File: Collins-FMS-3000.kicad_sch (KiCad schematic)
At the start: 29 parts, among them U2 MCP23017_SO, U3 MCP23017_SO, U4 IS31FL3733B

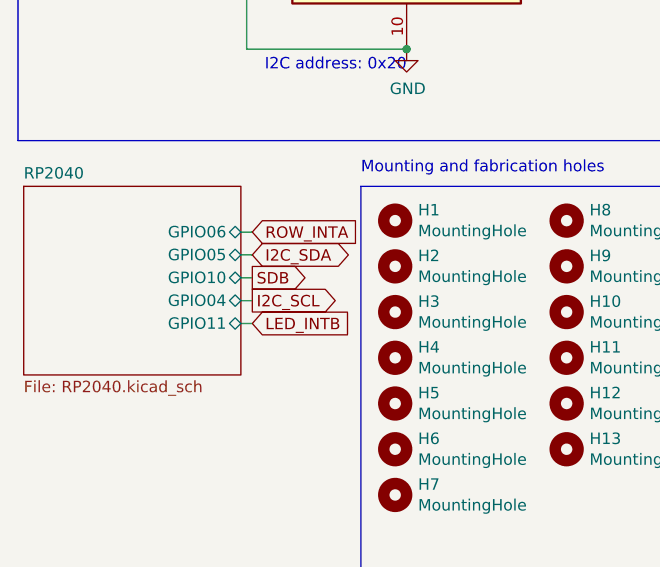
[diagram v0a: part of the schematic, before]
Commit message: Correct pin assignment for I2C, add via stitching
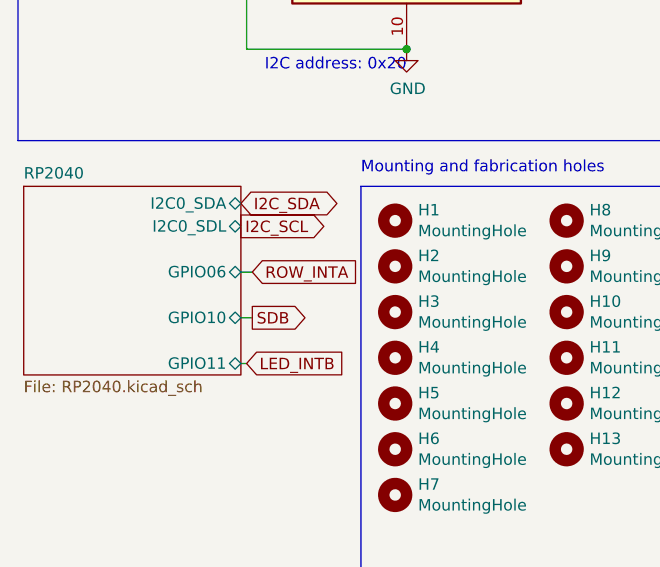
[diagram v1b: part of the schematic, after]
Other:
- sheet RP2040 ports: added I2C0_SDA, I2C0_SDL; removed GPIO04, GPIO05
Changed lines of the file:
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@@
     (stroke (width 0) (type default) (color 0 0 0 0))
   )
-  (wire (pts (xy 38.735 101.6) (xy 40.005 101.6))
+  (wire (pts (xy 38.735 106.045) (xy 40.005 106.045))
     (stroke (width 0) (type default) (color 0 0 0 0))
   )
@@
     (stroke (width 0) (type default) (color 0 0 0 0))
   )
-  (wire (pts (xy 38.735 106.68) (xy 40.005 106.68))
+  (wire (pts (xy 38.735 111.125) (xy 40.005 111.125))
     (stroke (width 0) (type default) (color 0 0 0 0))
   )
@@
     (stroke (width 0) (type default) (color 0 0 0 0))
   )
-  (wire (pts (xy 40.005 109.22) (xy 38.735 109.22))
-    (stroke (width 0) (type default) (color 0 0 0 0))
-  )
   (wire (pts (xy 148.59 27.94) (xy 153.67 27.94))
     (stroke (width 0) (type default) (color 0 0 0 0))
@@
     (stroke (width 0) (type default) (color 0 0 0 0))
   )
-  (wire (pts (xy 38.735 104.14) (xy 40.005 104.14))
-    (stroke (width 0) (type default) (color 0 0 0 0))
-  )
   (wire (pts (xy 148.59 22.86) (xy 138.43 22.86))
     (stroke (width 0) (type default) (color 0 0 0 0))
@@
     (stroke (width 0) (type default) (color 0 0 0 0))
   )
-  (wire (pts (xy 40.005 111.76) (xy 38.735 111.76))
+  (wire (pts (xy 39.37 116.205) (xy 38.735 116.205))
     (stroke (width 0) (type default) (color 0 0 0 0))
   )
@@
     )
   )
-  (global_label "LED_INTB" (shape input) (at 40.005 111.76 0) (fields_autoplaced)
+  (global_label "LED_INTB" (shape input) (at 39.37 116.205 0) (fields_autoplaced)
     (effects (font (size 1.27 1.27)) (justify left))
-    (property "Intersheet References" "${INTERSHEET_REFS}" (id 0) (at 0.635 1.27 0)
+    (property "Intersheet References" "${INTERSHEET_REFS}" (id 0) (at 0 5.715 0)
       (effects (font (size 1.27 1.27)) hide)
     )
@@
     )
   )
-  (global_label "ROW_INTA" (shape input) (at 40.005 101.6 0) (fields_autoplaced)
+  (global_label "ROW_INTA" (shape input) (at 40.005 106.045 0) (fields_autoplaced)
     (effects (font (size 1.27 1.27)) (justify left))
-    (property "Intersheet References" "${INTERSHEET_REFS}" (id 0) (at 0.635 -11.43 0)
+    (property "Intersheet References" "${INTERSHEET_REFS}" (id 0) (at 0.635 -6.985 0)
       (effects (font (size 1.27 1.27)) hide)
     )
@@
     )
   )
-  (global_label "I2C_SDA" (shape bidirectional) (at 40.005 104.14 0) (fields_autoplaced)
+  (global_label "I2C_SDA" (shape bidirectional) (at 38.735 98.425 0) (fields_autoplaced)
     (effects (font (size 1.27 1.27)) (justify left))
-    (property "Intersheet References" "${INTERSHEET_REFS}" (id 0) (at 0.635 1.27 0)
-      (effects (font (size 1.27 1.27)) hide)
-    )
-  )
-  (global_label "I2C_SCL" (shape output) (at 40.005 109.22 0) (fields_autoplaced)
+    (property "Intersheet References" "${INTERSHEET_REFS}" (id 0) (at -0.635 -4.445 0)
+      (effects (font (size 1.27 1.27)) hide)
+    )
+  )
+  (global_label "I2C_SCL" (shape output) (at 38.735 100.965 0) (fields_autoplaced)
     (effects (font (size 1.27 1.27)) (justify left))
-    (property "Intersheet References" "${INTERSHEET_REFS}" (id 0) (at 0.635 3.81 0)
-      (effects (font (size 1.27 1.27)) hide)
-    )
-  )
-  (global_label "SDB" (shape output) (at 40.005 106.68 0) (fields_autoplaced)
+    (property "Intersheet References" "${INTERSHEET_REFS}" (id 0) (at -0.635 -4.445 0)
+      (effects (font (size 1.27 1.27)) hide)
+    )
+  )
+  (global_label "SDB" (shape output) (at 40.005 111.125 0) (fields_autoplaced)
     (effects (font (size 1.27 1.27)) (justify left))
-    (property "Intersheet References" "${INTERSHEET_REFS}" (id 0) (at 0.635 -1.27 0)
+    (property "Intersheet References" "${INTERSHEET_REFS}" (id 0) (at 0.635 3.175 0)
       (effects (font (size 1.27 1.27)) hide)
     )
@@
       (effects (font (size 1.27 1.27)) (justify left top))
     )
-    (pin "GPIO06" bidirectional (at 38.735 101.6 0)
-      (effects (font (size 1.27 1.27)) (justify right))
-    )
-    (pin "GPIO05" bidirectional (at 38.735 104.14 0)
-      (effects (font (size 1.27 1.27)) (justify right))
-    )
-    (pin "GPIO04" bidirectional (at 38.735 109.22 0)
-      (effects (font (size 1.27 1.27)) (justify right))
-    )
-    (pin "GPIO11" bidirectional (at 38.735 111.76 0)
-      (effects (font (size 1.27 1.27)) (justify right))
-    )
-    (pin "GPIO10" bidirectional (at 38.735 106.68 0)
-      (effects (font (size 1.27 1.27)) (justify right))
-    )
+    (pin "GPIO06" bidirectional (at 38.735 106.045 0)
+      (effects (font (size 1.27 1.27)) (justify right))
+    )
+    (pin "GPIO11" bidirectional (at 38.735 116.205 0)
+      (effects (font (size 1.27 1.27)) (justify right))
+    )
+    (pin "GPIO10" bidirectional (at 38.735 111.125 0)
+      (effects (font (size 1.27 1.27)) (justify right))
+    )
+    (pin "I2C0_SDL" bidirectional (at 38.735 100.965 0)
+      (effects (font (size 1.27 1.27)) (justify right))
+    )
+    (pin "I2C0_SDA" bidirectional (at 38.735 98.425 0)
+      (effects (font (size 1.27 1.27)) (justify right))
+    )

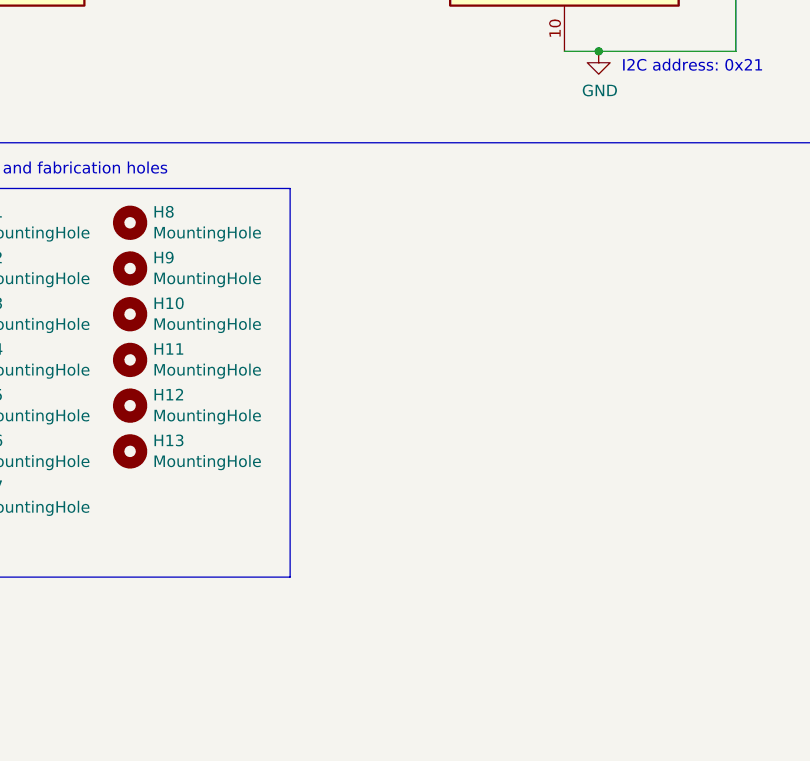
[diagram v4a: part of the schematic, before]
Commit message: Add test points
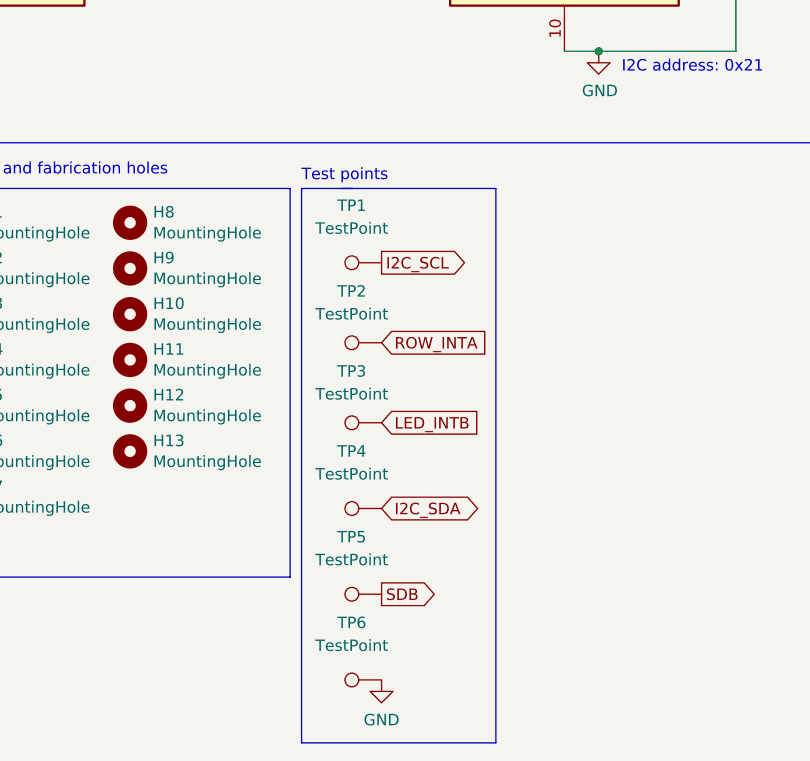
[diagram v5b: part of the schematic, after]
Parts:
- added TP1, TP2, TP3, TP4, TP5, TP6: TestPoint, TestPoint:TestPoint_Keystone_5005-5009_Compact, symbol Connector:TestPoint
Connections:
- net GND: now also TP6.1
- net I2C_SCL: now also TP1.1
- net I2C_SDA: now also TP4.1
- net LED_INTB: now also TP3.1
- net ROW_INTA: now also TP2.1
- net SDB: now also TP5.1
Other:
- note added: "Test points"
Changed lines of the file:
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@@
+    (stroke (width 0) (type default) (color 0 0 0 0))
+  )
+  (polyline (pts (xy 93.98 96.52) (xy 93.98 158.115))
     (stroke (width 0) (type default) (color 0 0 0 0))
   )
@@
     (stroke (width 0) (type default) (color 0 0 0 0))
   )
+  (polyline (pts (xy 99.695 96.52) (xy 93.98 96.52))
+    (stroke (width 0) (type default) (color 0 0 0 0))
+  )
   (wire (pts (xy 101.6 40.64) (xy 105.41 40.64))
     (stroke (width 0) (type default) (color 0 0 0 0))
@@
     (stroke (width 0) (type default) (color 0 0 0 0))
   )
+  (polyline (pts (xy 93.98 158.115) (xy 115.57 158.115))
+    (stroke (width 0) (type default) (color 0 0 0 0))
+  )
   (wire (pts (xy 214.63 62.23) (xy 222.25 62.23))
     (stroke (width 0) (type default) (color 0 0 0 0))
@@
     (stroke (width 0) (type default) (color 0 0 0 0))
   )
+  (polyline (pts (xy 98.425 96.52) (xy 115.57 96.52))
+    (stroke (width 0) (type default) (color 0 0 0 0))
+  )
   (wire (pts (xy 182.88 33.02) (xy 172.72 33.02))
     (stroke (width 0) (type default) (color 0 0 0 0))
@@
   )
   (polyline (pts (xy 52.07 96.52) (xy 92.71 96.52))
+    (stroke (width 0) (type default) (color 0 0 0 0))
+  )
+  (polyline (pts (xy 115.57 158.115) (xy 115.57 96.52))
     (stroke (width 0) (type default) (color 0 0 0 0))
   )
@@
     (effects (font (size 1.27 1.27)) (justify right bottom))
   )
+  (text "Test points" (at 93.98 95.885 0)
+    (effects (font (size 1.27 1.27)) (justify left bottom))
+  )
   (text "Button matrix" (at 13.97 15.24 0)
     (effects (font (size 1.27 1.27)) (justify left bottom))
@@
   (text "Backlight LEDs" (at 160.02 15.24 0)
     (effects (font (size 1.27 1.27)) (justify left bottom))
+  )
+  (global_label "I2C_SCL" (shape output) (at 102.87 104.775 0) (fields_autoplaced)
+    (effects (font (size 1.27 1.27)) (justify left))
+    (property "Intersheet References" "${INTERSHEET_REFS}" (id 0) (at 112.7537 104.6956 0)
+      (effects (font (size 1.27 1.27)) (justify left) hide)
+    )
   )
   (global_label "I2C_SCL" (shape input) (at 140.97 35.56 0) (fields_autoplaced)
@@
     )
   )
+  (global_label "I2C_SDA" (shape bidirectional) (at 102.87 132.08 0) (fields_autoplaced)
+    (effects (font (size 1.27 1.27)) (justify left))
+    (property "Intersheet References" "${INTERSHEET_REFS}" (id 0) (at 112.8142 132.0006 0)
+      (effects (font (size 1.27 1.27)) (justify left) hide)
+    )
+  )
   (global_label "LED_INTB" (shape input) (at 39.37 116.205 0) (fields_autoplaced)
     (effects (font (size 1.27 1.27)) (justify left))
@@
     )
   )
+  (global_label "ROW_INTA" (shape input) (at 102.87 113.665 0) (fields_autoplaced)
+    (effects (font (size 1.27 1.27)) (justify left))
+    (property "Intersheet References" "${INTERSHEET_REFS}" (id 0) (at 114.2052 113.5856 0)
+      (effects (font (size 1.27 1.27)) (justify left) hide)
+    )
+  )
   (global_label "I2C_SDA" (shape bidirectional) (at 39.37 33.02 180) (fields_autoplaced)
     (effects (font (size 1.27 1.27)) (justify right))
@@
     )
   )
+  (global_label "SDB" (shape output) (at 102.87 141.605 0) (fields_autoplaced)
+    (effects (font (size 1.27 1.27)) (justify left))
+    (property "Intersheet References" "${INTERSHEET_REFS}" (id 0) (at 108.9437 141.5256 0)
+      (effects (font (size 1.27 1.27)) (justify left) hide)
+    )
+  )
   (global_label "ROW_INTA" (shape input) (at 40.005 106.045 0) (fields_autoplaced)
     (effects (font (size 1.27 1.27)) (justify left))
@@
     (property "Intersheet References" "${INTERSHEET_REFS}" (id 0) (at 0 0 0)
       (effects (font (size 1.27 1.27)) hide)
+    )
+  )
+  (global_label "LED_INTB" (shape input) (at 102.87 122.555 0) (fields_autoplaced)
+    (effects (font (size 1.27 1.27)) (justify left))
+    (property "Intersheet References" "${INTERSHEET_REFS}" (id 0) (at 113.7818 122.4756 0)
+      (effects (font (size 1.27 1.27)) (justify left) hide)
     )
   )
@@
     (pin "1")
   )
+  (symbol (lib_id "Connector:TestPoint") (at 102.87 122.555 90) (unit 1)
+    (in_bom yes) (on_board yes) (fields_autoplaced)
+    (property "Reference" "TP3" (id 0) (at 99.568 116.84 90))
+    (property "Value" "TestPoint" (id 1) (at 99.568 119.38 90))
+    (property "Footprint" "TestPoint:TestPoint_Keystone_5005-5009_Compact" (id 2) (at 102.87 117.475 0)
+      (effects (font (size 1.27 1.27)) hide)
+    )
+    (property "Datasheet" "~" (id 3) (at 102.87 117.475 0)
+      (effects (font (size 1.27 1.27)) hide)
+    )
+    (pin "1")
+  )
+  (symbol (lib_id "power:GND") (at 102.87 151.13 0) (unit 1)
+    (in_bom yes) (on_board yes) (fields_autoplaced)
+    (property "Reference" "#PWR01" (id 0) (at 102.87 157.48 0)
+      (effects (font (size 1.27 1.27)) hide)
+    )
+    (property "Value" "GND" (id 1) (at 102.87 155.575 0))
+    (property "Footprint" "" (id 2) (at 102.87 151.13 0)
+      (effects (font (size 1.27 1.27)) hide)
+    )
+    (property "Datasheet" "" (id 3) (at 102.87 151.13 0)
+      (effects (font (size 1.27 1.27)) hide)
+    )
+    (pin "1")
+  )
+  (symbol (lib_id "Connector:TestPoint") (at 102.87 104.775 90) (unit 1)
+    (in_bom yes) (on_board yes) (fields_autoplaced)
+    (property "Reference" "TP1" (id 0) (at 99.568 98.425 90))
+    (property "Value" "TestPoint" (id 1) (at 99.568 100.965 90))
+    (property "Footprint" "TestPoint:TestPoint_Keystone_5005-5009_Compact" (id 2) (at 102.87 99.695 0)
+      (effects (font (size 1.27 1.27)) hide)
+    )
+    (property "Datasheet" "~" (id 3) (at 102.87 99.695 0)
+      (effects (font (size 1.27 1.27)) hide)
+    )
+    (pin "1")
+  )
+  (symbol (lib_id "Connector:TestPoint") (at 102.87 151.13 90) (unit 1)
+    (in_bom yes) (on_board yes) (fields_autoplaced)
+    (property "Reference" "TP6" (id 0) (at 99.568 144.78 90))
+    (property "Value" "TestPoint" (id 1) (at 99.568 147.32 90))
+    (property "Footprint" "TestPoint:TestPoint_Keystone_5005-5009_Compact" (id 2) (at 102.87 146.05 0)
+      (effects (font (size 1.27 1.27)) hide)
+    )
+    (property "Datasheet" "~" (id 3) (at 102.87 146.05 0)
+      (effects (font (size 1.27 1.27)) hide)
+    )
+    (pin "1")
+  )
+  (symbol (lib_id "Connector:TestPoint") (at 102.87 141.605 90) (unit 1)
+    (in_bom yes) (on_board yes)
+    (property "Reference" "TP5" (id 0) (at 99.568 135.255 90))
+    (property "Value" "TestPoint" (id 1) (at 99.568 137.795 90))
+    (property "Footprint" "TestPoint:TestPoint_Keystone_5005-5009_Compact" (id 2) (at 102.87 136.525 0)
+      (effects (font (size 1.27 1.27)) hide)
+    )
+    (property "Datasheet" "~" (id 3) (at 102.87 136.525 0)
+      (effects (font (size 1.27 1.27)) hide)
+    )
+    (pin "1")
+  )
   (symbol (lib_id "power:+3V3") (at 57.15 22.86 0) (unit 1)
     (in_bom yes) (on_board yes) (fields_autoplaced)
@@
     )
     (property "Datasheet" "" (id 3) (at 57.15 22.86 0)
+      (effects (font (size 1.27 1.27)) hide)
+    )
+    (pin "1")
+  )
+  (symbol (lib_id "Connector:TestPoint") (at 102.87 113.665 90) (unit 1)
+    (in_bom yes) (on_board yes) (fields_autoplaced)
+    (property "Reference" "TP2" (id 0) (at 99.568 107.95 90))
+    (property "Value" "TestPoint" (id 1) (at 99.568 110.49 90))
+    (property "Footprint" "TestPoint:TestPoint_Keystone_5005-5009_Compact" (id 2) (at 102.87 108.585 0)
+      (effects (font (size 1.27 1.27)) hide)
+    )
+    (property "Datasheet" "~" (id 3) (at 102.87 108.585 0)
+      (effects (font (size 1.27 1.27)) hide)
+    )
+    (pin "1")
+  )
+  (symbol (lib_id "Connector:TestPoint") (at 102.87 132.08 90) (unit 1)
+    (in_bom yes) (on_board yes) (fields_autoplaced)
+    (property "Reference" "TP4" (id 0) (at 99.568 125.73 90))
+    (property "Value" "TestPoint" (id 1) (at 99.568 128.27 90))
+    (property "Footprint" "TestPoint:TestPoint_Keystone_5005-5009_Compact" (id 2) (at 102.87 127 0)
+      (effects (font (size 1.27 1.27)) hide)
+    )
+    (property "Datasheet" "~" (id 3) (at 102.87 127 0)
       (effects (font (size 1.27 1.27)) hide)
     )
@@
   )
   (symbol_instances
+    (path "/5dedf2e2-a6f3-4121-beb4-346ed207802e"
+      (reference "#PWR01") (unit 1) (value "GND") (footprint "")
+    )
     (path "/00000000-0000-0000-0000-0000626e7004"
       (reference "#PWR02") (unit 1) (value "GND") (footprint "")
@@
       (reference "SW69") (unit 2) (value "SW_Push_LED") (footprint "Collins-FMS-3000:SW_PUSH_6mm")
     )
+    (path "/61fa851c-0703-4688-bf0f-9cc32a6397f8"
+      (reference "TP1") (unit 1) (value "TestPoint") (footprint "TestPoint:TestPoint_Keystone_5005-5009_Compact")
+    )
+    (path "/e47ee89e-f990-4adc-8af1-d6262d5b9d81"
+      (reference "TP2") (unit 1) (value "TestPoint") (footprint "TestPoint:TestPoint_Keystone_5005-5009_Compact")
+    )
+    (path "/5a3f5e9e-abdb-410b-9574-202dc674d476"
+      (reference "TP3") (unit 1) (value "TestPoint") (footprint "TestPoint:TestPoint_Keystone_5005-5009_Compact")
+    )
+    (path "/eae54dbc-fa4f-44a0-82fa-343b413abe9a"
+      (reference "TP4") (unit 1) (value "TestPoint") (footprint "TestPoint:TestPoint_Keystone_5005-5009_Compact")
+    )
+    (path "/d2c48699-040d-4a21-a5e0-4cf96efacb51"
+      (reference "TP5") (unit 1) (value "TestPoint") (footprint "TestPoint:TestPoint_Keystone_5005-5009_Compact")
+    )
+    (path "/6c308c8b-0904-449a-9612-5d51cca11a5f"
+      (reference "TP6") (unit 1) (value "TestPoint") (footprint "TestPoint:TestPoint_Keystone_5005-5009_Compact")
+    )
     (path "/dc0d5261-e4d2-4b54-8008-75fea26fa95d/3da426a9-d467-44e7-9a0d-d28f5f22ddf8"
